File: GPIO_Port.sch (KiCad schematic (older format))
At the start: 91 parts, among them J5 Conn_02x20_Odd_Even

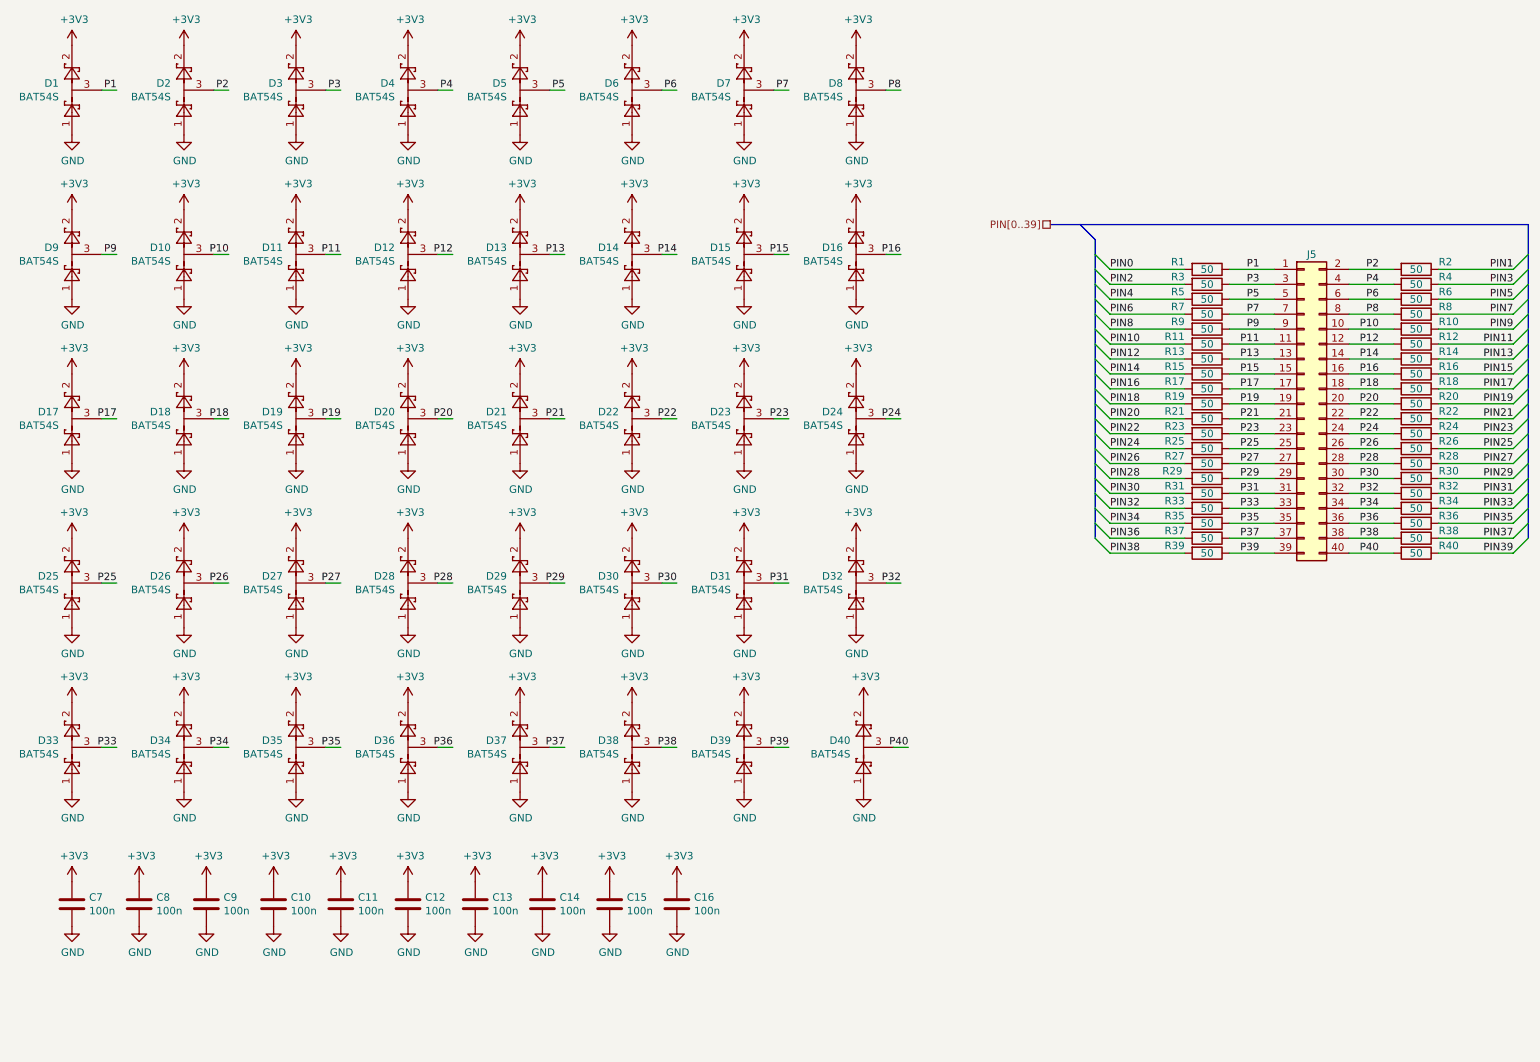
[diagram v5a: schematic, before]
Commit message: Reroute GPIO, 5V regulator, and I2C buffer
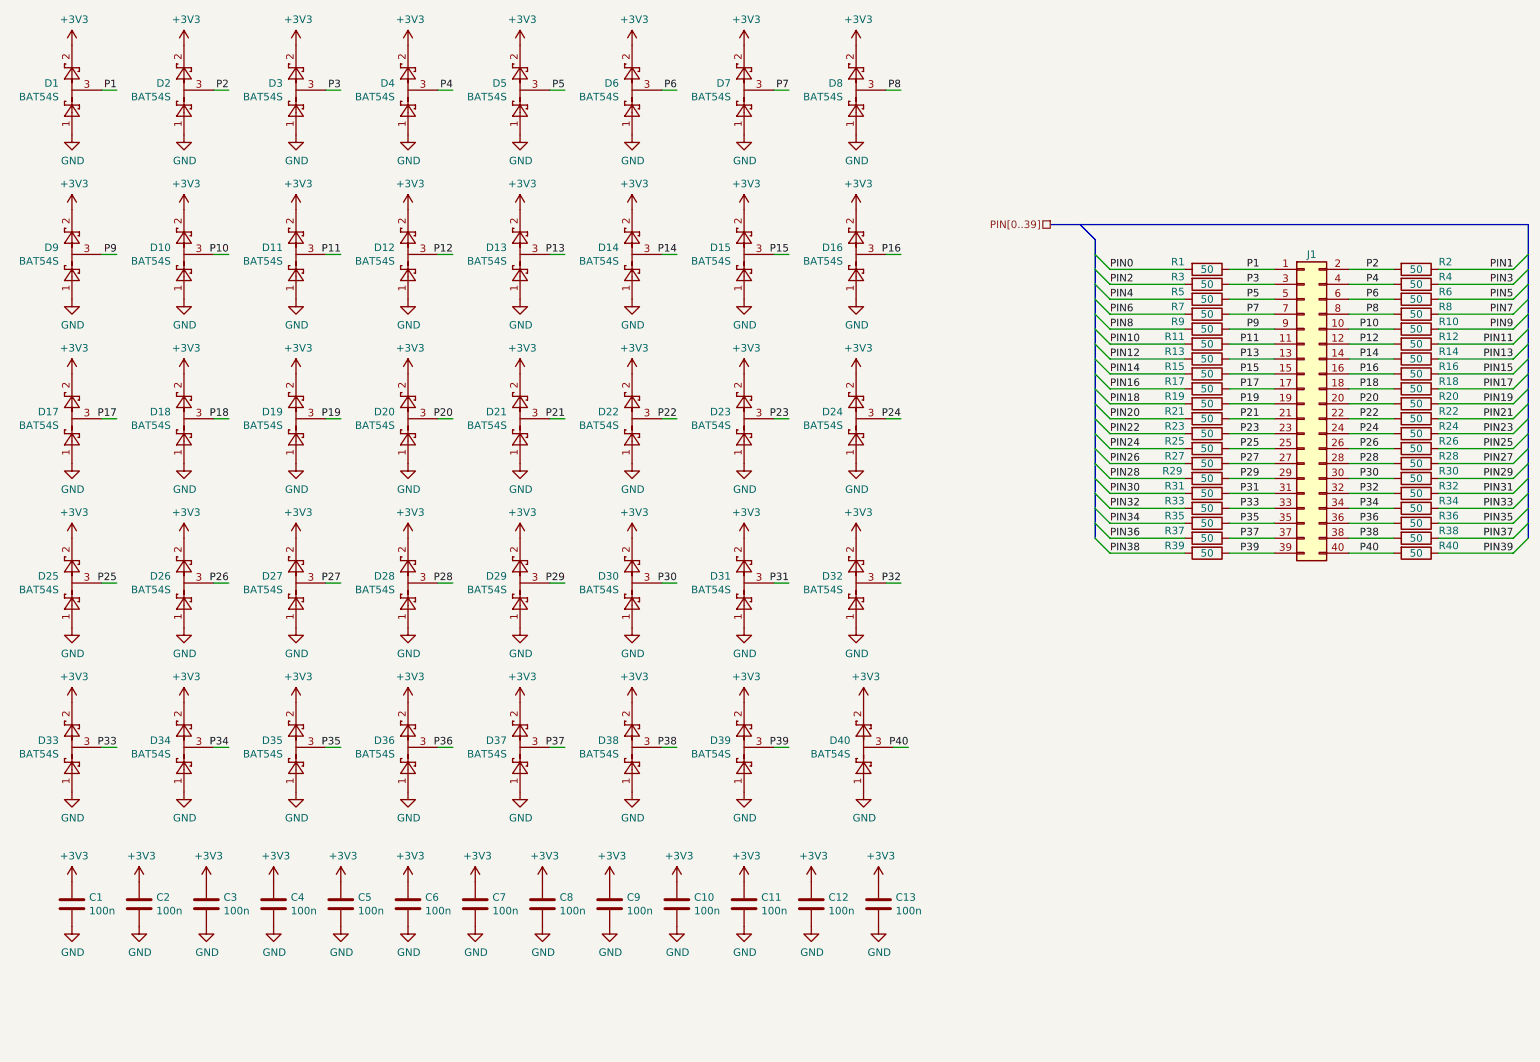
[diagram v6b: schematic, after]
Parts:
- added C11, C12, C13: 100n, Capacitor_SMD:C_0805_2012Metric, symbol Device:C
- D1, D10, D11, D12, D13, D14, D15, D16, D17, D18, D19, D2, D20, D21, D22, D23, D24, D25, D26, D27, D28, D29, D3, D30, D31, D32, D33, D34, D35, D36, D37, D38, D39, D4, D40, D5, D6, D7, D8, D9: footprint Package_TO_SOT_SMD:SOT-23 -> Package_TO_SOT_SMD:SOT-323_SC-70
- renumbered C7 to C1, C16 to C10, C8 to C2, C9 to C3, C10 to C4, C11 to C5, C12 to C6, C13 to C7, C14 to C8, C15 to C9, J5 to J1
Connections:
- net +3V3: now also C11.1, C12.1, C13.1
- net GND: now also C11.2, C12.2, C13.2
